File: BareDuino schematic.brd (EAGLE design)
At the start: 49.5 x 50.8 mm, 33 parts, among them IC1 7805TV, X1 HC49-HC49-3L

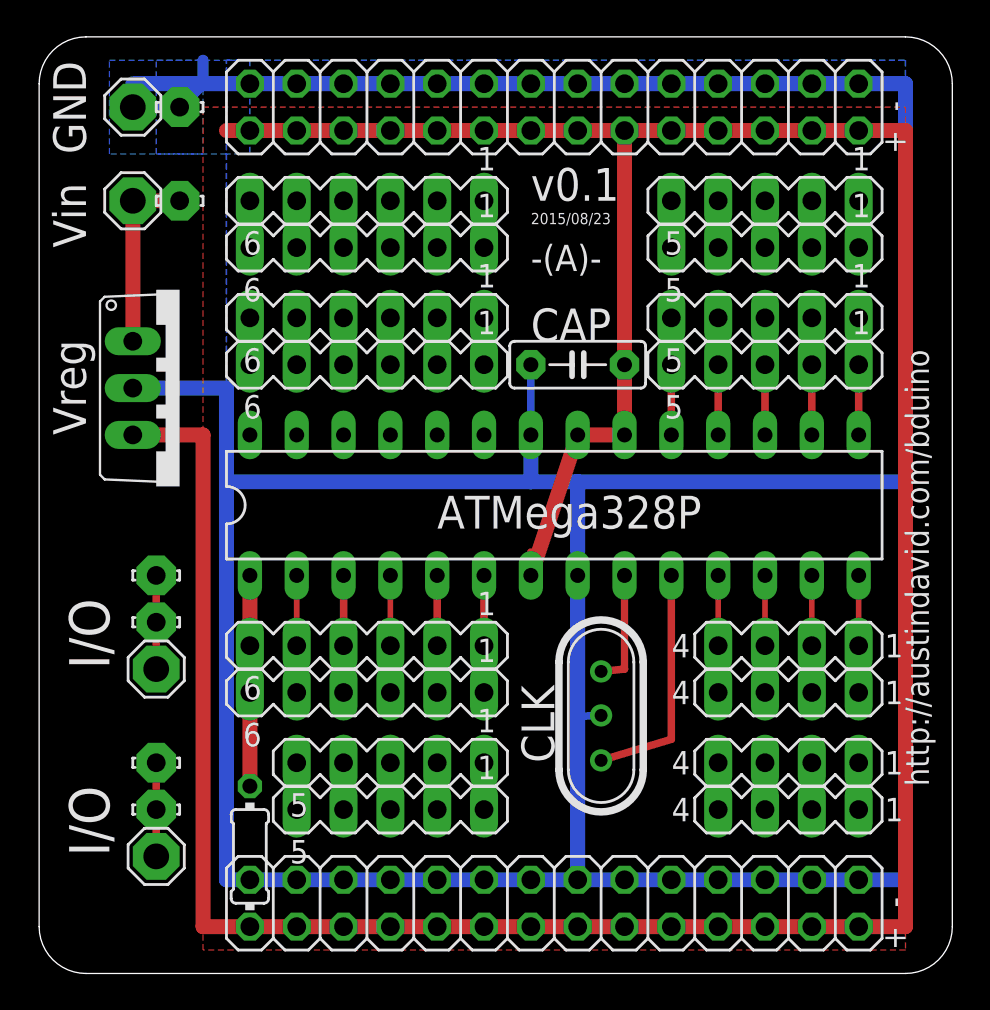
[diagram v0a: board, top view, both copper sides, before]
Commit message: update! cleanup + servos + FTDI
fixes missing traces, realigns the breakout pads to make *all* of them
servo-friendly, adds an FTDI header, and adds labels on (most) pins
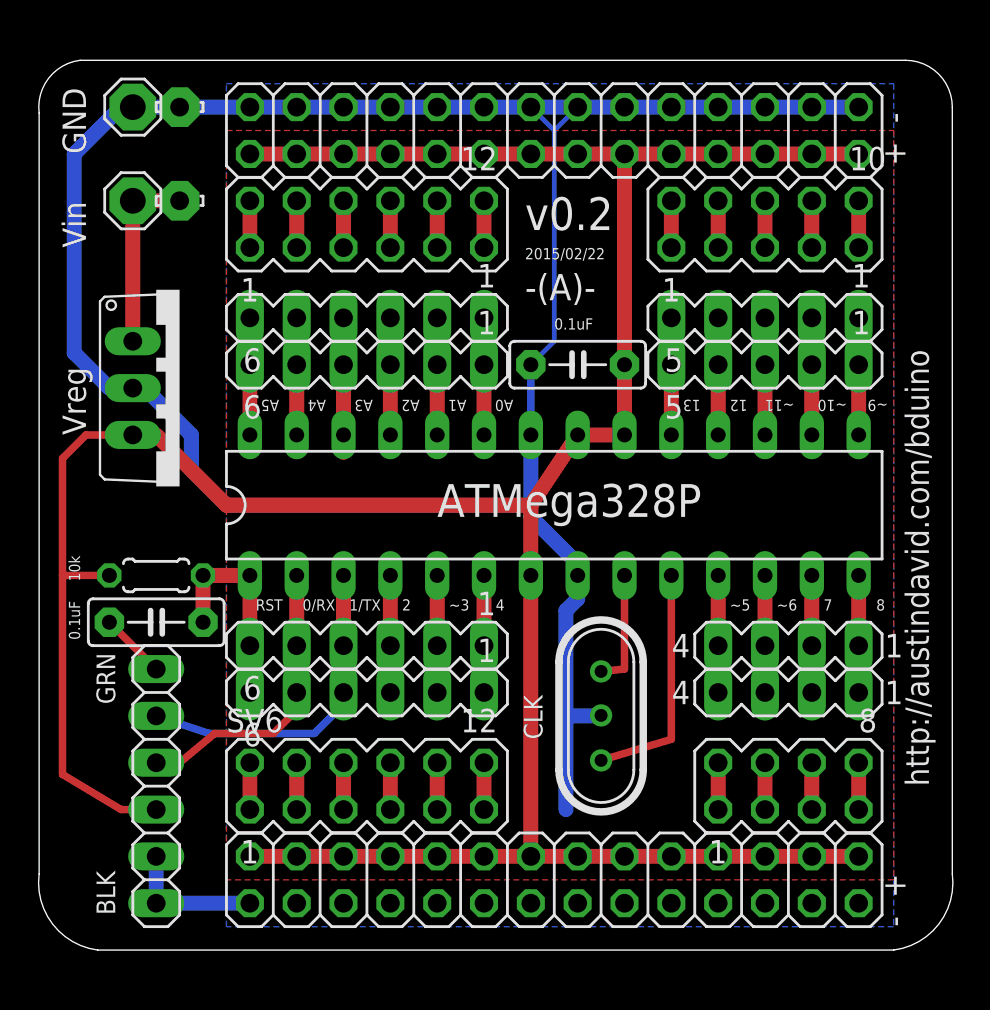
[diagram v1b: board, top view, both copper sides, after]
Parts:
- removed LSP1, LSP5: SE14, solpad:SE14
- removed LSP6, LSP7, LSP8, LSP9: LSP10, solpad:LSP10
- removed SV10, SV9: (no value), con-lstb:MA04-1
- removed SV13, SV14: (no value), con-lstb:MA05-1
- added C2: (no value), capacitor-wima:C5B2.5
- added JP2: (no value), pinhead:1X06
- R1: device resistor:0204/7 -> rcl:0204/5
- SV3: device con-lstb:MA05-1 -> con-lstb:MA05-2
- SV4: device con-lstb:MA05-1 -> con-lstb:MA04-2
- SV5, SV6: device con-lstb:MA06-1 -> con-lstb:MA06-2
- moved SV6 31.8 mm to (40.6, 25.4), turned to 0 degrees
- moved SV4 22.9 mm to (63.5, 25.4), turned to 0 degrees
- moved R1 16.1 mm to (29.2, 36.8), turned to 180 degrees
- moved SV5 7.62 mm to (40.6, 55.9), turned to 0 degrees
- moved SV1 6.35 mm to (62.2, 50.8)
- moved SV11 6.35 mm to (63.5, 33.0)
- moved SV12 6.35 mm to (63.5, 30.5)
- moved SV2 6.35 mm to (62.2, 48.3)
- moved SV3 5.08 mm to (62.2, 55.9), turned to 0 degrees
- moved SV7 3.81 mm to (40.6, 50.8)
- moved SV8 2.54 mm to (40.6, 48.3)
- moved JP1 1.27 mm to (50.8, 20.3), turned to 180 degrees
- moved JP3 1.27 mm to (50.8, 61.0)
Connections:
- removed net IO1: LSP1.MP, LSP6.MP, LSP7.MP
- removed net IO2: LSP5.MP, LSP8.MP, LSP9.MP
- new net N$21: C2.1, JP2.1
- new net N$22: SV6.1, SV6.2
- net DIP15: now also SV1.1, SV2.1; no longer SV3.1, SV4.1
- net DIP16: now also SV1.2, SV2.2; no longer SV3.2, SV4.2
- net DIP17: now also SV1.3, SV2.3; no longer SV3.3, SV4.3
- net DIP18: now also SV1.4, SV2.4; no longer SV3.4, SV4.4
- net DIP19: now also SV1.5, SV2.5; no longer SV3.5, SV4.5
- net DIP2: now also JP2.3
- net DIP3: now also JP2.2
- net GND: now also JP2.5, JP2.6
- net N$1: now also SV5.11, SV5.12; no longer SV5.6, SV6.6
- net N$10: now also SV4.1, SV4.2; no longer SV1.2, SV2.2
- net N$11: now also SV6.11, SV6.12; no longer SV1.1, SV2.1
- net N$12: now also SV3.5, SV3.6; no longer SV13.5, SV14.5
- net N$13: now also SV3.7, SV3.8; no longer SV13.4, SV14.4
- net N$14: now also SV3.10, SV3.9; no longer SV13.3, SV14.3
- net N$15: now also SV3.3, SV3.4; no longer SV13.2, SV14.2
- net N$16: now also SV3.1, SV3.2; no longer SV13.1, SV14.1
- net N$17: now also SV6.10, SV6.9; no longer SV10.4, SV9.4
- net N$18: now also SV6.7, SV6.8; no longer SV10.3, SV9.3
- net N$19: now also SV6.5, SV6.6; no longer SV10.2, SV9.2
- net N$2: now also SV5.10, SV5.9; no longer SV5.5, SV6.5
- net N$20: now also SV6.3, SV6.4; no longer SV10.1, SV9.1
- net N$3: now also SV5.7, SV5.8; no longer SV5.4, SV6.4
- net N$4: now also SV5.5, SV5.6; no longer SV5.3, SV6.3
- net N$5: now also SV5.3, SV5.4; no longer SV5.2, SV6.2
- net N$6: now also SV5.2; no longer SV6.1
- net N$7: now also SV4.7, SV4.8; no longer SV1.5, SV2.5
- net N$8: now also SV4.5, SV4.6; no longer SV1.4, SV2.4
- net N$9: now also SV4.3, SV4.4; no longer SV1.3, SV2.3
- net RST: now also C2.2
- net VCC: now also JP2.4
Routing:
- net GND: track 314.2 -> 167.9 mm
- net VCC: track 246.8 -> 179.3 mm
- net DIP3: track 6.35 -> 24.0 mm
- net DIP2: track 6.35 -> 17.3 mm
- net DIP26: track 0.00 -> 10.3 mm
- net DIP24: track 0.00 -> 10.2 mm
- net DIP27: track 0.00 -> 9.52 mm
- net DIP23: track 0.00 -> 9.52 mm
- net DIP28: track 0.00 -> 8.89 mm
- net DIP25: track 0.00 -> 8.89 mm
- net DIP6: track 6.35 -> 13.0 mm
- net DIP5: track 6.35 -> 12.7 mm
- net IO2: track 5.08 -> 0.00 mm
- net IO1: track 5.08 -> 0.00 mm
- net DIP18: track 6.35 -> 10.2 mm
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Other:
- board size 49.5 x 50.8 mm -> 49.6 x 48.3 mm
- board text added: "- +"
- board text added: "0.1uF"
- board text added: "0/RX"
- board text added: "1/TX"
- board text added: "10k"
- board text added: "12"
- board text added: "13"
- board text added: "2"
- board text added: "2015/02/22"
- board text added: "4"
- board text added: "7"
- board text added: "8"
- board text added: "A0"
- board text added: "A1"
- board text added: "A2"
- board text added: "A3"
- board text added: "A4"
- board text added: "A5"
- board text added: "BLK"
- board text added: "GRN"
- board text added: "RST"
- board text added: "v0.2"
- board text added: "~10"
- board text added: "~11"
- board text added: "~3"
- board text added: "~5"
- board text added: "~6"
- board text added: "~9"
- board text removed: "2015/08/23"
- board text removed: "CAP"
- board text removed: "I/O"
- board text removed: "v0.1"
